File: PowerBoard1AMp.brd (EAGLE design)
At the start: 11.9 x 27.6 mm, 4 parts, among them IC1 VREG

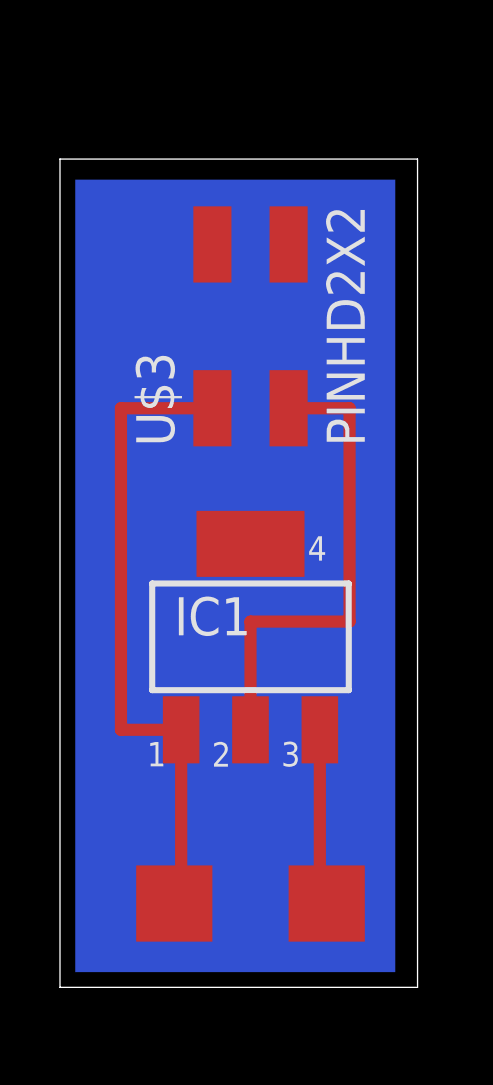
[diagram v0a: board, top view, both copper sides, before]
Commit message: Added two capacitors for regulators
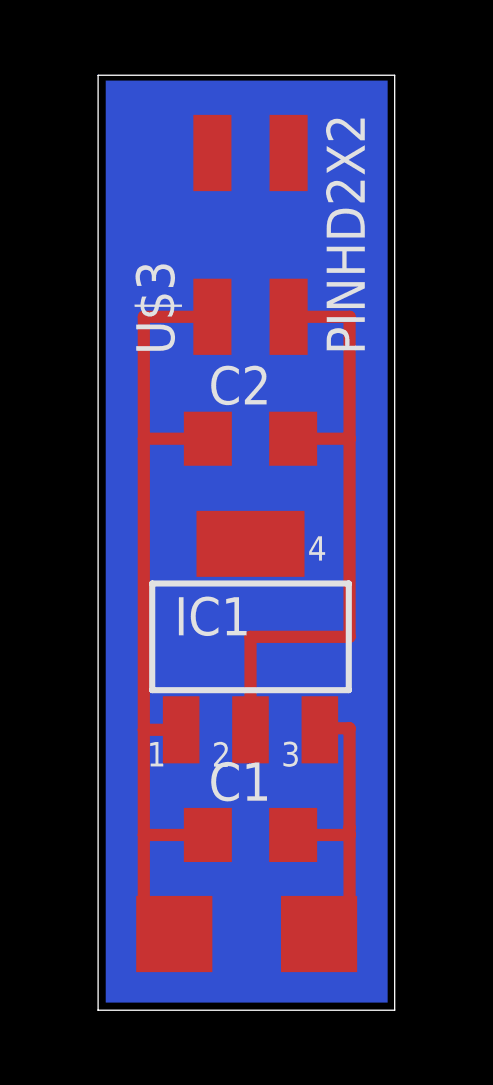
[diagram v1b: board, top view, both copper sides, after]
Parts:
- added C1, C2: 10uF, fablab:1206
- moved U$3 3.05 mm to (24.1, 25.9)
- moved U$2 1.05 mm to (26.4, 2.79)
- moved U$1 1.02 mm to (21.6, 2.79)
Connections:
- net GND: now also C1.1, C2.1
- net N$2: now also C2.2
- net N$4: now also C1.2
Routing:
- net GND: track 21.8 -> 29.4 mm
- net N$2: track 16.1 -> 21.0 mm
- net N$4: track 6.02 -> 10.8 mm
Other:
- board size 11.9 x 27.6 mm -> 9.9 x 31.2 mm
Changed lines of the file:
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@@
 <?xml version="1.0" encoding="utf-8"?>
 <!DOCTYPE eagle SYSTEM "eagle.dtd">
-<eagle version="6.3">
+<eagle version="7.3.0">
 <drawing>
 <settings>
@@
 <setting verticaltext="up"/>
 </settings>
-<grid distance="20" unitdist="mil" unit="mil" style="lines" multiple="1" display="yes" altdistance="0.025" altunitdist="inch" altunit="inch"/>
+<grid distance="10" unitdist="mil" unit="mil" style="lines" multiple="1" display="yes" altdistance="0.025" altunitdist="inch" altunit="inch"/>
 <layers>
 <layer number="1" name="Top" color="4" fill="1" visible="no" active="yes"/>
@@
 <layer number="97" name="Info" color="7" fill="1" visible="no" active="no"/>
 <layer number="98" name="Guide" color="6" fill="1" visible="no" active="no"/>
+<layer number="99" name="SpiceOrder" color="7" fill="1" visible="no" active="no"/>
 <layer number="100" name="Muster" color="7" fill="1" visible="no" active="no"/>
 <layer number="101" name="Patch_Top" color="12" fill="4" visible="no" active="yes"/>
@@
 <layer number="111" name="LPC17xx" color="7" fill="1" visible="no" active="yes"/>
 <layer number="112" name="tSilk" color="7" fill="1" visible="no" active="yes"/>
+<layer number="113" name="IDFDebug" color="4" fill="1" visible="no" active="yes"/>
 <layer number="116" name="Patch_BOT" color="9" fill="4" visible="no" active="yes"/>
 <layer number="121" name="_tsilk" color="7" fill="1" visible="no" active="yes"/>
@@
 <board>
 <plain>
-<wire x1="17.78" y1="1.016" x2="29.698" y2="1.016" width="0" layer="20"/>
-<wire x1="29.698" y1="1.016" x2="29.698" y2="28.626" width="0" layer="20"/>
-<wire x1="29.698" y1="28.626" x2="17.78" y2="28.626" width="0" layer="20"/>
-<wire x1="17.78" y1="28.626" x2="17.78" y2="1.016" width="0" layer="20"/>
-<rectangle x1="18.288" y1="1.524" x2="28.956" y2="27.94" layer="16"/>
+<wire x1="19.05" y1="0.254" x2="28.936" y2="0.254" width="0" layer="20"/>
+<wire x1="28.936" y1="0.254" x2="28.936" y2="31.42" width="0" layer="20"/>
+<wire x1="28.936" y1="31.42" x2="19.05" y2="31.42" width="0" layer="20"/>
+<wire x1="19.05" y1="31.42" x2="19.05" y2="0.254" width="0" layer="20"/>
+<rectangle x1="19.304" y1="0.508" x2="28.702" y2="31.242" layer="16"/>
 </plain>
 <attributes>
@@
 <pass name="Default">
 <param name="RoutingGrid" value="50mil"/>
+<param name="AutoGrid" value="1"/>
+<param name="Efforts" value="0"/>
+<param name="TopRouterVariant" value="1"/>
 <param name="tpViaShape" value="round"/>
 <param name="PrefDir.1" value="|"/>
@@
 </autorouter>
 <elements>
-<element name="U$3" library="fabPatil" package="2X02SMD" value="PINHD2X2" x="24.13" y="22.86" rot="R90"/>
+<element name="U$3" library="fabPatil" package="2X02SMD" value="PINHD2X2" x="24.13" y="25.908" rot="R90"/>
 <element name="IC1" library="fabPatil" package="SOT223" value="VREG" x="24.13" y="12.7"/>
-<element name="U$1" library="ng" package="PAD.1" value="" x="21.59" y="3.81"/>
-<element name="U$2" library="ng" package="PAD.1" value="SIGNAL" x="26.67" y="3.81"/>
+<element name="U$1" library="ng" package="PAD.1" value="" x="21.59" y="2.794"/>
+<element name="U$2" library="ng" package="PAD.1" value="SIGNAL" x="26.416" y="2.794"/>
+<element name="C1" library="fablab" package="1206" value="10uF" x="24.13" y="6.096"/>
+<element name="C2" library="fablab" package="1206" value="10uF" x="24.13" y="19.304"/>
 </elements>
 <signals>
@@
 <contactref element="U$3" pad="1"/>
 <contactref element="U$1" pad="P$1"/>
-<wire x1="21.59" y1="3.81" x2="21.8186" y2="3.81" width="0.4064" layer="1"/>
-<wire x1="21.8186" y1="3.81" x2="21.8186" y2="9.6012" width="0.4064" layer="1"/>
-<wire x1="21.8186" y1="9.6012" x2="19.812" y2="9.6012" width="0.4064" layer="1"/>
-<wire x1="19.812" y1="9.6012" x2="19.812" y2="20.32" width="0.4064" layer="1"/>
-<wire x1="19.812" y1="20.32" x2="22.86" y2="20.32" width="0.4064" layer="1"/>
+<wire x1="21.8186" y1="9.6012" x2="20.574" y2="9.6012" width="0.4064" layer="1"/>
+<wire x1="20.574" y1="9.6012" x2="20.574" y2="19.304" width="0.4064" layer="1"/>
+<contactref element="C1" pad="1"/>
+<contactref element="C2" pad="1"/>
+<wire x1="22.708" y1="19.304" x2="20.574" y2="19.304" width="0.4064" layer="1"/>
+<wire x1="22.86" y1="23.368" x2="20.574" y2="23.368" width="0.4064" layer="1"/>
+<wire x1="20.574" y1="23.368" x2="20.574" y2="19.304" width="0.4064" layer="1"/>
+<wire x1="21.59" y1="2.794" x2="20.574" y2="2.794" width="0.4064" layer="1"/>
+<wire x1="20.574" y1="2.794" x2="20.574" y2="6.096" width="0.4064" layer="1"/>
+<wire x1="20.574" y1="6.096" x2="20.574" y2="9.6012" width="0.4064" layer="1"/>
+<wire x1="22.708" y1="6.096" x2="20.574" y2="6.096" width="0.4064" layer="1"/>
 </signal>
 <signal name="N$2">
 <contactref element="IC1" pad="2"/>
 <contactref element="U$3" pad="3"/>
-<wire x1="24.13" y1="9.6012" x2="24.13" y2="13.208" width="0.4064" layer="1"/>
-<wire x1="24.13" y1="13.208" x2="27.432" y2="13.208" width="0.4064" layer="1"/>
-<wire x1="27.432" y1="13.208" x2="27.432" y2="20.32" width="0.4064" layer="1"/>
-<wire x1="27.432" y1="20.32" x2="25.4" y2="20.32" width="0.4064" layer="1"/>
+<wire x1="24.13" y1="9.6012" x2="24.13" y2="12.7" width="0.4064" layer="1"/>
+<wire x1="24.13" y1="12.7" x2="27.432" y2="12.7" width="0.4064" layer="1"/>
+<wire x1="27.432" y1="12.7" x2="27.432" y2="19.304" width="0.4064" layer="1"/>
+<contactref element="C2" pad="2"/>
+<wire x1="25.552" y1="19.304" x2="27.432" y2="19.304" width="0.4064" layer="1"/>
+<wire x1="25.4" y1="23.368" x2="27.432" y2="23.368" width="0.4064" layer="1"/>
+<wire x1="27.432" y1="23.368" x2="27.432" y2="19.304" width="0.4064" layer="1"/>
 </signal>
 <signal name="N$4">
 <contactref element="U$2" pad="P$1"/>
 <contactref element="IC1" pad="3"/>
-<wire x1="26.67" y1="3.81" x2="26.4414" y2="3.81" width="0.4064" layer="1"/>
-<wire x1="26.4414" y1="3.81" x2="26.4414" y2="9.6012" width="0.4064" layer="1"/>
+<contactref element="C1" pad="2"/>
+<wire x1="26.416" y1="2.794" x2="27.432" y2="2.794" width="0.4064" layer="1"/>
+<wire x1="27.432" y1="2.794" x2="27.432" y2="6.096" width="0.4064" layer="1"/>
+<wire x1="27.432" y1="6.35" x2="27.432" y2="9.652" width="0.4064" layer="1"/>
+<wire x1="27.432" y1="9.652" x2="26.4414" y2="9.652" width="0.4064" layer="1"/>
+<wire x1="26.4414" y1="9.652" x2="26.4414" y2="9.6012" width="0.4064" layer="1"/>
+<wire x1="25.552" y1="6.096" x2="27.432" y2="6.096" width="0.4064" layer="1"/>
+<wire x1="27.432" y1="6.096" x2="27.432" y2="6.35" width="0.4064" layer="1"/>
 </signal>
 </signals>

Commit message: chaning the board boundry thickness
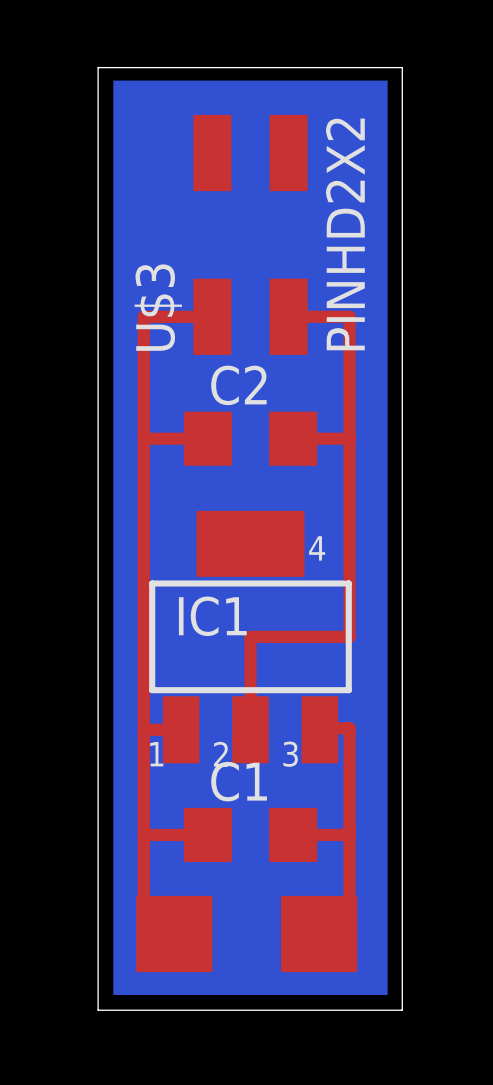
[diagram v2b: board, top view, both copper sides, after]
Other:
- board size 9.9 x 31.2 mm -> 10.1 x 31.4 mm

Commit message: Change the pins for VCC and GND in connector
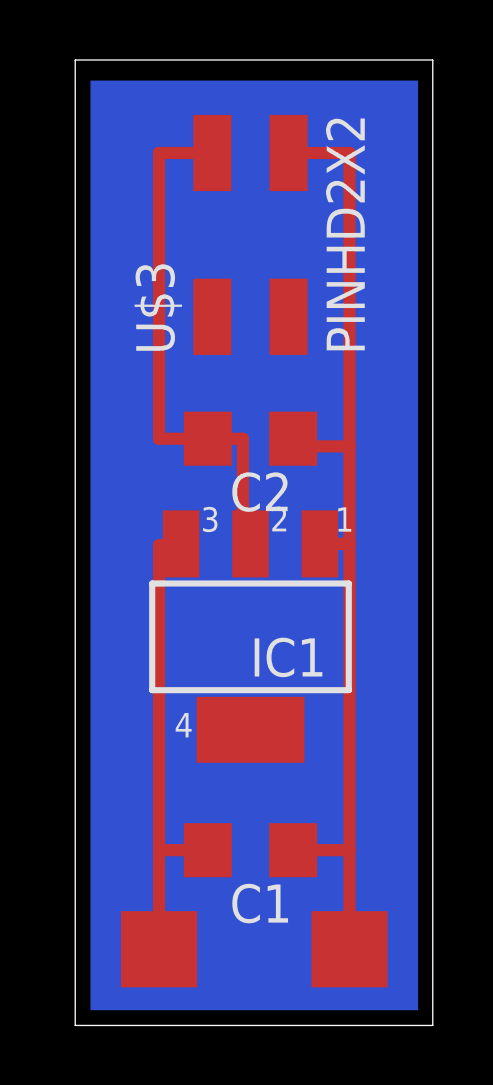
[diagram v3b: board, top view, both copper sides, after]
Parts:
- moved U$1 5.86 mm to (27.4, 2.29)
- moved U$2 5.36 mm to (21.1, 2.29)
- moved C1 0.51 mm to (24.1, 5.59), turned to 180 degrees
- turned C2 to 180 degrees
- turned IC1 to 180 degrees
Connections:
- removed net N$2: C2.2, IC1.2, U$3.3
- removed net RX: U$3.4
- removed net TX: U$3.2
- new net VCC: C2.2, IC1.2, U$3.2
- net GND: now also U$3.4; no longer U$3.1
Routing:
- net N$2: track 21.0 -> 0.00 mm
- net VCC: track 0.00 -> 17.9 mm
- net N$4: track 10.8 -> 15.9 mm
- net GND: track 29.4 -> 34.1 mm
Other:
- board size 10.1 x 31.4 mm -> 11.9 x 32.2 mm
